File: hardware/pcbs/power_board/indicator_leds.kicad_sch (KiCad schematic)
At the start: 10 parts

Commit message: power_board: finalise all footprints
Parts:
- gave numbers to parts that had none: 10
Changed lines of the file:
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@@
   (symbol (lib_id "Transistor_FET:BSS138") (at 151.13 132.08 0) (unit 1)
     (in_bom yes) (on_board yes) (dnp no)
-    (property "Reference" "Q?" (at 147.32 128.27 0)
+    (property "Reference" "Q4" (at 147.32 128.27 0)
       (effects (font (size 1.27 1.27)) (justify left))
     )
@@
       (project "power_board"
         (path "/4b166175-80a4-48c6-994d-6e62a6160b87/9db409a6-3616-4139-9d4b-1b510fbe4a7d"
-          (reference "Q?") (unit 1)
+          (reference "Q4") (unit 1)
         )
       )
@@
   (symbol (lib_id "Device:R") (at 123.19 96.52 90) (unit 1)
     (in_bom yes) (on_board yes) (dnp no)
-    (property "Reference" "R?" (at 123.19 93.98 90)
+    (property "Reference" "R37" (at 123.19 93.98 90)
       (effects (font (size 1.27 1.27)))
     )
@@
       (project "power_board"
         (path "/4b166175-80a4-48c6-994d-6e62a6160b87/9db409a6-3616-4139-9d4b-1b510fbe4a7d"
-          (reference "R?") (unit 1)
+          (reference "R37") (unit 1)
         )
       )
@@
   (symbol (lib_id "Device:R") (at 123.19 132.08 90) (unit 1)
     (in_bom yes) (on_board yes) (dnp no)
-    (property "Reference" "R?" (at 123.19 129.54 90)
+    (property "Reference" "R39" (at 123.19 129.54 90)
       (effects (font (size 1.27 1.27)))
     )
@@
       (project "power_board"
         (path "/4b166175-80a4-48c6-994d-6e62a6160b87/9db409a6-3616-4139-9d4b-1b510fbe4a7d"
-          (reference "R?") (unit 1)
+          (reference "R39") (unit 1)
         )
       )
@@
   (symbol (lib_id "extra:LED_RYG") (at 148.59 85.09 270) (mirror x) (unit 1)
     (in_bom yes) (on_board yes) (dnp no)
-    (property "Reference" "D?" (at 161.29 80.01 90)
+    (property "Reference" "D2" (at 161.29 80.01 90)
       (effects (font (size 1.27 1.27)) (justify right))
     )
@@
       (project "power_board"
         (path "/4b166175-80a4-48c6-994d-6e62a6160b87/9db409a6-3616-4139-9d4b-1b510fbe4a7d"
-          (reference "D?") (unit 1)
+          (reference "D2") (unit 1)
         )
       )
@@
   (symbol (lib_id "power:+5V") (at 143.51 58.42 0) (mirror y) (unit 1)
     (in_bom yes) (on_board yes) (dnp no) (fields_autoplaced)
-    (property "Reference" "#PWR025" (at 143.51 62.23 0)
+    (property "Reference" "#PWR070" (at 143.51 62.23 0)
       (effects (font (size 1.27 1.27)) hide)
     )
@@
       (project "power_board"
         (path "/4b166175-80a4-48c6-994d-6e62a6160b87/9db409a6-3616-4139-9d4b-1b510fbe4a7d"
-          (reference "#PWR025") (unit 1)
+          (reference "#PWR070") (unit 1)
         )
       )
@@
   (symbol (lib_id "Device:R") (at 153.67 64.77 0) (mirror x) (unit 1)
     (in_bom yes) (on_board yes) (dnp no)
-    (property "Reference" "R?" (at 152.4 60.96 0)
+    (property "Reference" "R42" (at 152.4 60.96 0)
       (effects (font (size 1.27 1.27)) (justify right))
     )
@@
       (project "power_board"
         (path "/4b166175-80a4-48c6-994d-6e62a6160b87/9db409a6-3616-4139-9d4b-1b510fbe4a7d"
-          (reference "R?") (unit 1)
+          (reference "R42") (unit 1)
         )
       )
@@
   (symbol (lib_id "power:+5V") (at 148.59 58.42 0) (mirror y) (unit 1)
     (in_bom yes) (on_board yes) (dnp no) (fields_autoplaced)
-    (property "Reference" "#PWR027" (at 148.59 62.23 0)
+    (property "Reference" "#PWR072" (at 148.59 62.23 0)
       (effects (font (size 1.27 1.27)) hide)
     )
@@
       (project "power_board"
         (path "/4b166175-80a4-48c6-994d-6e62a6160b87/9db409a6-3616-4139-9d4b-1b510fbe4a7d"
-          (reference "#PWR027") (unit 1)
+          (reference "#PWR072") (unit 1)
         )
       )
@@
   (symbol (lib_id "Device:R") (at 148.59 64.77 0) (mirror x) (unit 1)
     (in_bom yes) (on_board yes) (dnp no)
-    (property "Reference" "R?" (at 147.32 60.96 0)
+    (property "Reference" "R41" (at 147.32 60.96 0)
       (effects (font (size 1.27 1.27)) (justify right))
     )
@@
       (project "power_board"
         (path "/4b166175-80a4-48c6-994d-6e62a6160b87/9db409a6-3616-4139-9d4b-1b510fbe4a7d"
-          (reference "R?") (unit 1)
+          (reference "R41") (unit 1)
         )
       )
@@
   (symbol (lib_id "power:+5V") (at 153.67 58.42 0) (mirror y) (unit 1)
     (in_bom yes) (on_board yes) (dnp no) (fields_autoplaced)
-    (property "Reference" "#PWR029" (at 153.67 62.23 0)
+    (property "Reference" "#PWR074" (at 153.67 62.23 0)
       (effects (font (size 1.27 1.27)) hide)
     )
@@
       (project "power_board"
         (path "/4b166175-80a4-48c6-994d-6e62a6160b87/9db409a6-3616-4139-9d4b-1b510fbe4a7d"
-          (reference "#PWR029") (unit 1)
+          (reference "#PWR074") (unit 1)
         )
       )
@@
   (symbol (lib_id "power:GND") (at 143.51 102.87 0) (unit 1)
     (in_bom yes) (on_board yes) (dnp no) (fields_autoplaced)
-    (property "Reference" "#PWR026" (at 143.51 109.22 0)
+    (property "Reference" "#PWR071" (at 143.51 109.22 0)
       (effects (font (size 1.27 1.27)) hide)
     )
@@
       (project "power_board"
         (path "/4b166175-80a4-48c6-994d-6e62a6160b87/9db409a6-3616-4139-9d4b-1b510fbe4a7d"
-          (reference "#PWR026") (unit 1)
+          (reference "#PWR071") (unit 1)
         )
       )
@@
   (symbol (lib_id "Device:R") (at 123.19 114.3 90) (unit 1)
     (in_bom yes) (on_board yes) (dnp no)
-    (property "Reference" "R?" (at 123.19 111.76 90)
+    (property "Reference" "R38" (at 123.19 111.76 90)
       (effects (font (size 1.27 1.27)))
     )
@@
       (project "power_board"
         (path "/4b166175-80a4-48c6-994d-6e62a6160b87/9db409a6-3616-4139-9d4b-1b510fbe4a7d"
-          (reference "R?") (unit 1)
+          (reference "R38") (unit 1)
         )
       )
@@
   (symbol (lib_id "power:GND") (at 148.59 120.65 0) (unit 1)
     (in_bom yes) (on_board yes) (dnp no) (fields_autoplaced)
-    (property "Reference" "#PWR028" (at 148.59 127 0)
+    (property "Reference" "#PWR073" (at 148.59 127 0)
       (effects (font (size 1.27 1.27)) hide)
     )
@@
       (project "power_board"
         (path "/4b166175-80a4-48c6-994d-6e62a6160b87/9db409a6-3616-4139-9d4b-1b510fbe4a7d"
-          (reference "#PWR028") (unit 1)
+          (reference "#PWR073") (unit 1)
         )
       )
@@
   (symbol (lib_id "Transistor_FET:BSS138") (at 140.97 96.52 0) (unit 1)
     (in_bom yes) (on_board yes) (dnp no)
-    (property "Reference" "Q?" (at 137.16 92.71 0)
+    (property "Reference" "Q2" (at 137.16 92.71 0)
       (effects (font (size 1.27 1.27)) (justify left))
     )
@@
       (project "power_board"
         (path "/4b166175-80a4-48c6-994d-6e62a6160b87/9db409a6-3616-4139-9d4b-1b510fbe4a7d"
-          (reference "Q?") (unit 1)
+          (reference "Q2") (unit 1)
         )
       )
@@
   (symbol (lib_id "Device:R") (at 143.51 64.77 0) (mirror x) (unit 1)
     (in_bom yes) (on_board yes) (dnp no)
-    (property "Reference" "R?" (at 142.24 60.96 0)
+    (property "Reference" "R40" (at 142.24 60.96 0)
       (effects (font (size 1.27 1.27)) (justify right))
     )
@@
       (project "power_board"
         (path "/4b166175-80a4-48c6-994d-6e62a6160b87/9db409a6-3616-4139-9d4b-1b510fbe4a7d"
-          (reference "R?") (unit 1)
+          (reference "R40") (unit 1)
         )
       )
@@
   (symbol (lib_id "Transistor_FET:BSS138") (at 146.05 114.3 0) (unit 1)
     (in_bom yes) (on_board yes) (dnp no)
-    (property "Reference" "Q?" (at 142.24 110.49 0)
+    (property "Reference" "Q3" (at 142.24 110.49 0)
       (effects (font (size 1.27 1.27)) (justify left))
     )
@@
       (project "power_board"
         (path "/4b166175-80a4-48c6-994d-6e62a6160b87/9db409a6-3616-4139-9d4b-1b510fbe4a7d"
-          (reference "Q?") (unit 1)
-        )
-      )
+          (reference "Q3") (unit 1)
+        )
+      )

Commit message: power_board: final version
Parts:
- Q2, Q3, Q4: LCSC (none) -> C7420339
- R37, R38, R39: LCSC (none) -> C17415
- R40, R41, R42: LCSC (none) -> C17398
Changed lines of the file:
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@@
+			)
+		)
+		(property "LCSC" "C7420339"
+			(at 151.13 132.08 0)
+			(effects
+				(font
+					(size 1.27 1.27)
+				)
+				(hide yes)
 			)
 		)
@@
 			)
 		)
+		(property "LCSC" "C17415"
+			(at 123.19 96.52 0)
+			(effects
+				(font
+					(size 1.27 1.27)
+				)
+				(hide yes)
+			)
+		)
 		(pin "1"
 		)
@@
 		)
 		(property "Shop" "https://store.comet.bg/Catalogue/Product/29580/"
+			(at 123.19 132.08 0)
+			(effects
+				(font
+					(size 1.27 1.27)
+				)
+				(hide yes)
+			)
+		)
+		(property "LCSC" "C17415"
 			(at 123.19 132.08 0)
 			(effects
@@
 			)
 		)
+		(property "LCSC" "C17398"
+			(at 153.67 64.77 0)
+			(effects
+				(font
+					(size 1.27 1.27)
+				)
+				(hide yes)
+			)
+		)
 		(pin "2"
 		)
@@
 			)
 		)
+		(property "LCSC" "C17398"
+			(at 148.59 64.77 0)
+			(effects
+				(font
+					(size 1.27 1.27)
+				)
+				(hide yes)
+			)
+		)
 		(pin "2"
 		)
@@
 			)
 		)
+		(property "LCSC" "C17415"
+			(at 123.19 114.3 0)
+			(effects
+				(font
+					(size 1.27 1.27)
+				)
+				(hide yes)
+			)
+		)
 		(pin "1"
 		)
@@
 			)
 		)
+		(property "LCSC" "C7420339"
+			(at 140.97 96.52 0)
+			(effects
+				(font
+					(size 1.27 1.27)
+				)
+				(hide yes)
+			)
+		)
 		(pin "2"
 		)
@@
 			)
 		)
+		(property "LCSC" "C17398"
+			(at 143.51 64.77 0)
+			(effects
+				(font
+					(size 1.27 1.27)
+				)
+				(hide yes)
+			)
+		)
 		(pin "2"
 		)
@@
 			(at 146.05 114.3 0)
 			(effects
+				(font
+					(size 1.27 1.27)
+				)
+				(hide yes)
+			)
+		)
+		(property "LCSC" "C7420339"
+			(at 146.05 114.3 0)
+			(effects

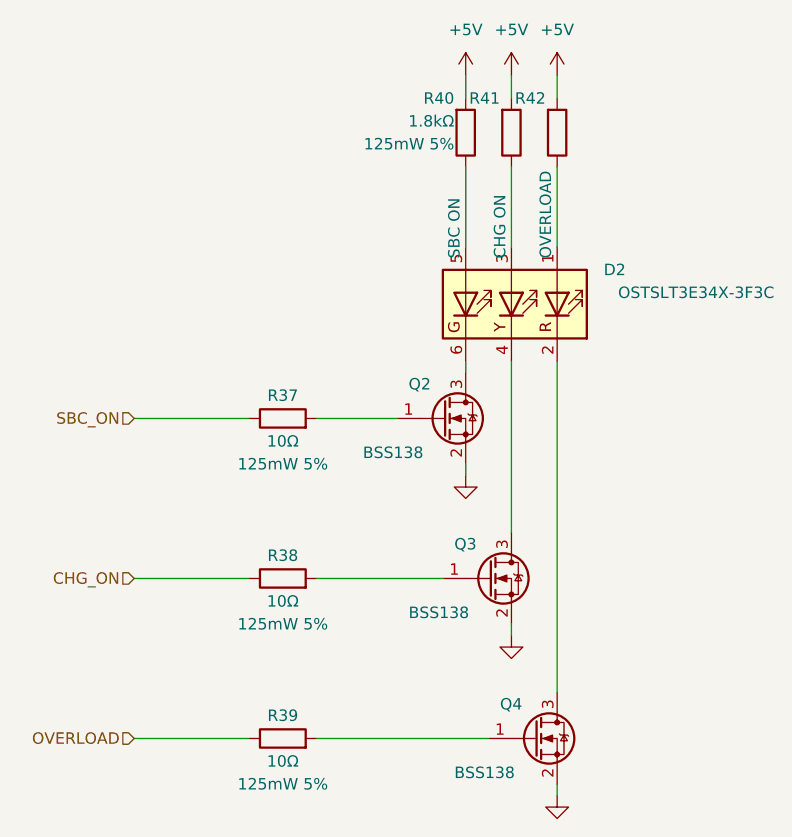
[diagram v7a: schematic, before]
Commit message: power_board: update components to new versions and annotate
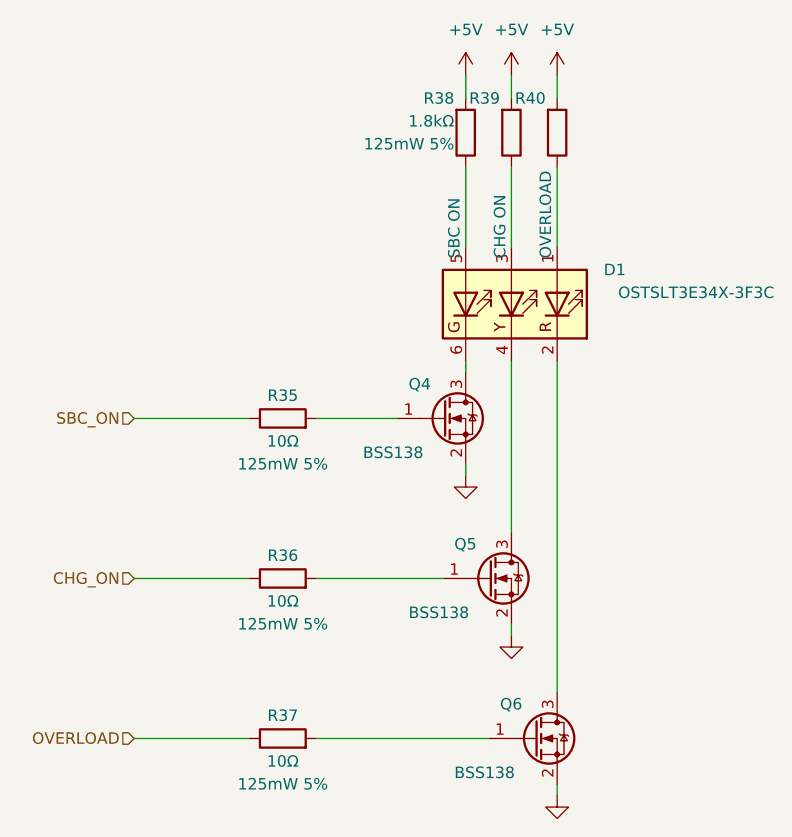
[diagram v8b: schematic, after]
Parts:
- D1: renamed from D2; Part (none) -> OSTSLT3E34X-3F3C
- Q4: renamed from Q2; Part (none) -> BSS138
- Q5: renamed from Q3; Part (none) -> BSS138
- Q6: renamed from Q4; Part (none) -> BSS138
- renumbered R37 to R35, R38 to R36, R39 to R37, R40 to R38, R41 to R39, R42 to R40
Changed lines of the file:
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@@
 		(on_board yes)
 		(dnp no)
-		(property "Reference" "Q4"
+		(property "Reference" "Q6"
 			(at 147.32 128.27 0)
 			(effects
@@
 			)
 		)
+		(property "Part" "BSS138"
+			(at 151.13 132.08 0)
+			(effects
+				(font
+					(size 1.27 1.27)
+				)
+				(hide yes)
+			)
+		)
 		(pin "2"
 		)
@@
 			(project "power_board"
 				(path "/4b166175-80a4-48c6-994d-6e62a6160b87/9db409a6-3616-4139-9d4b-1b510fbe4a7d"
-					(reference "Q4")
+					(reference "Q6")
 					(unit 1)
 				)
@@
 		(on_board yes)
 		(dnp no)
-		(property "Reference" "R37"
+		(property "Reference" "R35"
 			(at 123.19 93.98 90)
 			(effects
@@
 			(project "power_board"
 				(path "/4b166175-80a4-48c6-994d-6e62a6160b87/9db409a6-3616-4139-9d4b-1b510fbe4a7d"
-					(reference "R37")
+					(reference "R35")
 					(unit 1)
 				)
@@
 		(on_board yes)
 		(dnp no)
-		(property "Reference" "R39"
+		(property "Reference" "R37"
 			(at 123.19 129.54 90)
 			(effects
@@
 			(project "power_board"
 				(path "/4b166175-80a4-48c6-994d-6e62a6160b87/9db409a6-3616-4139-9d4b-1b510fbe4a7d"
-					(reference "R39")
+					(reference "R37")
 					(unit 1)
 				)
@@
 		(on_board yes)
 		(dnp no)
-		(property "Reference" "D2"
+		(property "Reference" "D1"
 			(at 161.29 80.01 90)
 			(effects
@@
 			)
 		)
+		(property "Part" "OSTSLT3E34X-3F3C"
+			(at 148.59 85.09 0)
+			(effects
+				(font
+					(size 1.27 1.27)
+				)
+				(hide yes)
+			)
+		)
 		(pin "4"
 		)
@@
 			(project "power_board"
 				(path "/4b166175-80a4-48c6-994d-6e62a6160b87/9db409a6-3616-4139-9d4b-1b510fbe4a7d"
-					(reference "D2")
+					(reference "D1")
 					(unit 1)
 				)
@@
 		(dnp no)
 		(fields_autoplaced yes)
-		(property "Reference" "#PWR060"
+		(property "Reference" "#PWR059"
 			(at 143.51 62.23 0)
 			(effects
@@
 			(project "power_board"
 				(path "/4b166175-80a4-48c6-994d-6e62a6160b87/9db409a6-3616-4139-9d4b-1b510fbe4a7d"
-					(reference "#PWR060")
+					(reference "#PWR059")
 					(unit 1)
 				)
@@
 		(on_board yes)
 		(dnp no)
-		(property "Reference" "R42"
+		(property "Reference" "R40"
 			(at 152.4 60.96 0)
 			(effects
@@
 			(project "power_board"
 				(path "/4b166175-80a4-48c6-994d-6e62a6160b87/9db409a6-3616-4139-9d4b-1b510fbe4a7d"
-					(reference "R42")
+					(reference "R40")
 					(unit 1)
 				)
@@
 		(dnp no)
 		(fields_autoplaced yes)
-		(property "Reference" "#PWR065"
+		(property "Reference" "#PWR064"
 			(at 153.67 144.78 0)
 			(effects
@@
 			(project "power_board"
 				(path "/4b166175-80a4-48c6-994d-6e62a6160b87/9db409a6-3616-4139-9d4b-1b510fbe4a7d"
-					(reference "#PWR065")
+					(reference "#PWR064")
 					(unit 1)
 				)
@@
 		(dnp no)
 		(fields_autoplaced yes)
-		(property "Reference" "#PWR062"
+		(property "Reference" "#PWR061"
 			(at 148.59 62.23 0)
 			(effects
@@
 			(project "power_board"
 				(path "/4b166175-80a4-48c6-994d-6e62a6160b87/9db409a6-3616-4139-9d4b-1b510fbe4a7d"
-					(reference "#PWR062")
+					(reference "#PWR061")
 					(unit 1)
 				)
@@
 		(on_board yes)
 		(dnp no)
-		(property "Reference" "R41"
+		(property "Reference" "R39"
 			(at 147.32 60.96 0)
 			(effects
@@
 			(project "power_board"
 				(path "/4b166175-80a4-48c6-994d-6e62a6160b87/9db409a6-3616-4139-9d4b-1b510fbe4a7d"
-					(reference "R41")
+					(reference "R39")
 					(unit 1)
 				)
@@
 		(dnp no)
 		(fields_autoplaced yes)
-		(property "Reference" "#PWR064"
+		(property "Reference" "#PWR063"
 			(at 153.67 62.23 0)
 			(effects
@@
 			(project "power_board"
 				(path "/4b166175-80a4-48c6-994d-6e62a6160b87/9db409a6-3616-4139-9d4b-1b510fbe4a7d"
-					(reference "#PWR064")
+					(reference "#PWR063")
 					(unit 1)
 				)
@@
 		(dnp no)
 		(fields_autoplaced yes)
-		(property "Reference" "#PWR061"
+		(property "Reference" "#PWR060"
 			(at 143.51 109.22 0)
 			(effects
@@
 			(project "power_board"
 				(path "/4b166175-80a4-48c6-994d-6e62a6160b87/9db409a6-3616-4139-9d4b-1b510fbe4a7d"
-					(reference "#PWR061")
+					(reference "#PWR060")
 					(unit 1)
 				)
@@
 		(on_board yes)
 		(dnp no)
-		(property "Reference" "R38"
+		(property "Reference" "R36"
 			(at 123.19 111.76 90)
 			(effects
@@
 			(project "power_board"
 				(path "/4b166175-80a4-48c6-994d-6e62a6160b87/9db409a6-3616-4139-9d4b-1b510fbe4a7d"
-					(reference "R38")
+					(reference "R36")
 					(unit 1)
 				)
@@
 		(dnp no)
 		(fields_autoplaced yes)
-		(property "Reference" "#PWR063"
+		(property "Reference" "#PWR062"
 			(at 148.59 127 0)
 			(effects
@@
 			(project "power_board"
 				(path "/4b166175-80a4-48c6-994d-6e62a6160b87/9db409a6-3616-4139-9d4b-1b510fbe4a7d"
-					(reference "#PWR063")
+					(reference "#PWR062")
 					(unit 1)
 				)
@@
 		(on_board yes)
 		(dnp no)
-		(property "Reference" "Q2"
+		(property "Reference" "Q4"
 			(at 137.16 92.71 0)
 			(effects
@@
 			)
 		)
+		(property "Part" "BSS138"
+			(at 140.97 96.52 0)
+			(effects
+				(font
+					(size 1.27 1.27)
+				)
+				(hide yes)
+			)
+		)
 		(pin "2"
 		)
@@
 			(project "power_board"
 				(path "/4b166175-80a4-48c6-994d-6e62a6160b87/9db409a6-3616-4139-9d4b-1b510fbe4a7d"
-					(reference "Q2")
+					(reference "Q4")
 					(unit 1)
 				)
@@
 		(on_board yes)
 		(dnp no)
-		(property "Reference" "R40"
+		(property "Reference" "R38"
 			(at 142.24 60.96 0)
 			(effects
@@
 			(project "power_board"
 				(path "/4b166175-80a4-48c6-994d-6e62a6160b87/9db409a6-3616-4139-9d4b-1b510fbe4a7d"
-					(reference "R40")
+					(reference "R38")
 					(unit 1)
 				)
@@
 		(on_board yes)
 		(dnp no)
-		(property "Reference" "Q3"
+		(property "Reference" "Q5"
 			(at 142.24 110.49 0)
 			(effects
@@
 			)
 		)
+		(property "Part" "BSS138"
+			(at 146.05 114.3 0)
+			(effects
+				(font
+					(size 1.27 1.27)
+				)
+				(hide yes)
+			)
+		)
 		(pin "2"
 		)
@@
 			(project "power_board"
 				(path "/4b166175-80a4-48c6-994d-6e62a6160b87/9db409a6-3616-4139-9d4b-1b510fbe4a7d"
-					(reference "Q3")
-					(unit 1)
-				)
+					(reference "Q5")
+					(unit 1)
+				)
